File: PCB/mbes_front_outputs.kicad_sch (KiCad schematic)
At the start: 54 parts, among them IC2 BDX34C, IC3 BDX34C, K1 RT42xxxx, Q1 D45VH10, Q10 BC337, Q11 BC337, Q12 BC327, Q13 BC337, Q14 D45VH10, Q15 D45VH10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

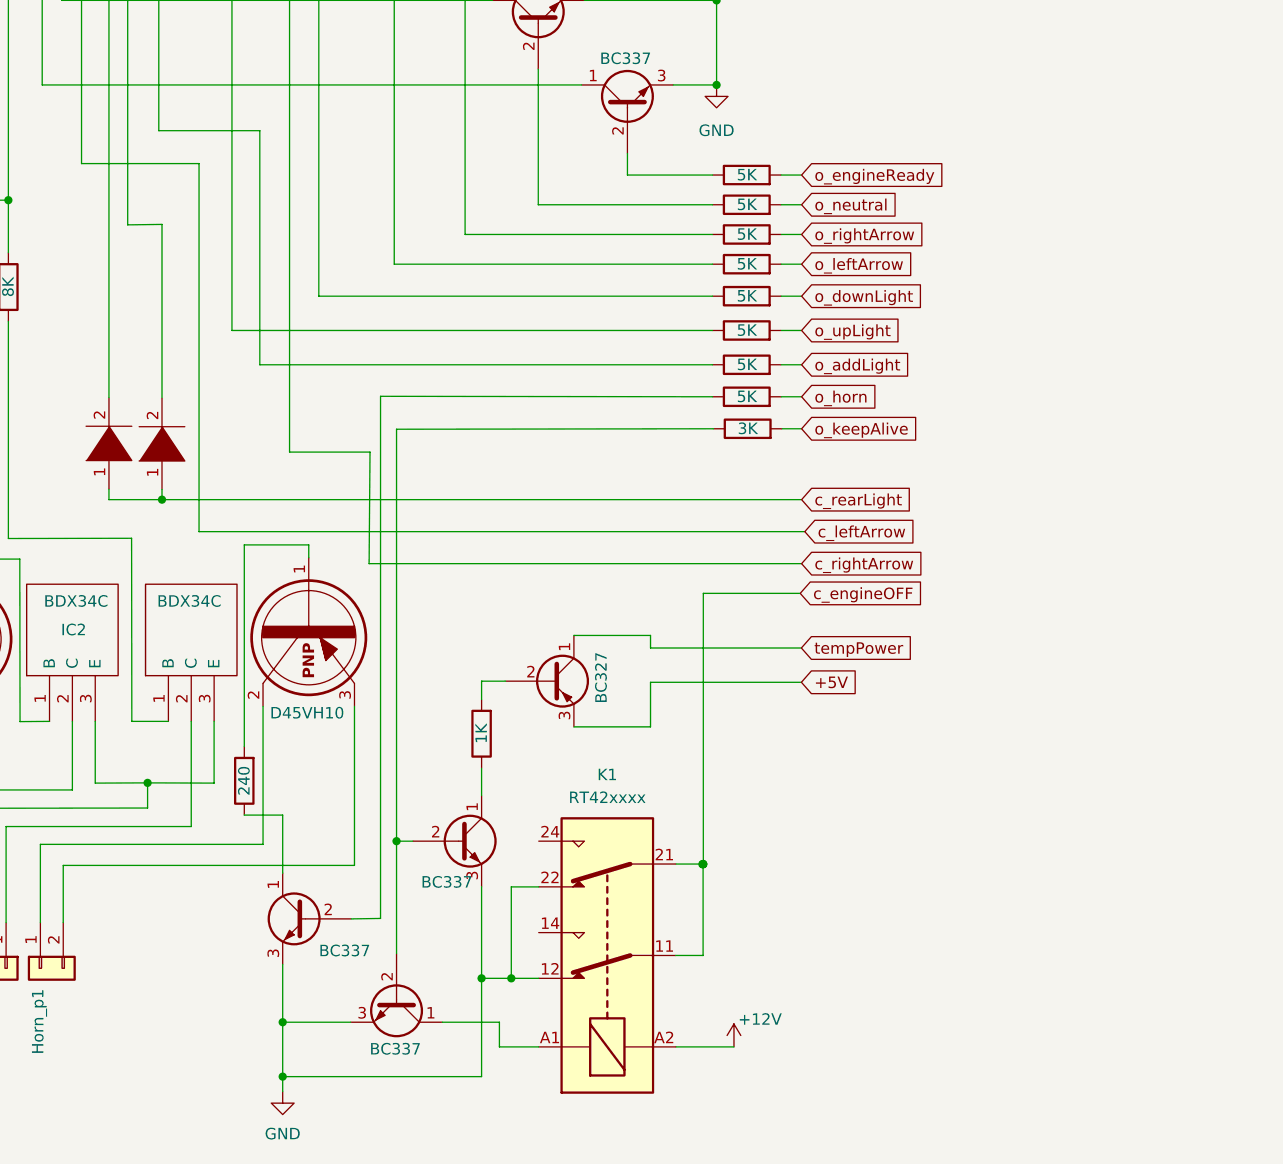
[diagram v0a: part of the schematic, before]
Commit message: feat: power-off button
Because MCU could have a problem for an unpredictable reason, a power-off button has been added to stop the current to the MCU.
But, because I am paranoide and the transistor could have problems, I connected the power-off button yo the MCU too. In this way
it can always shutdown itself
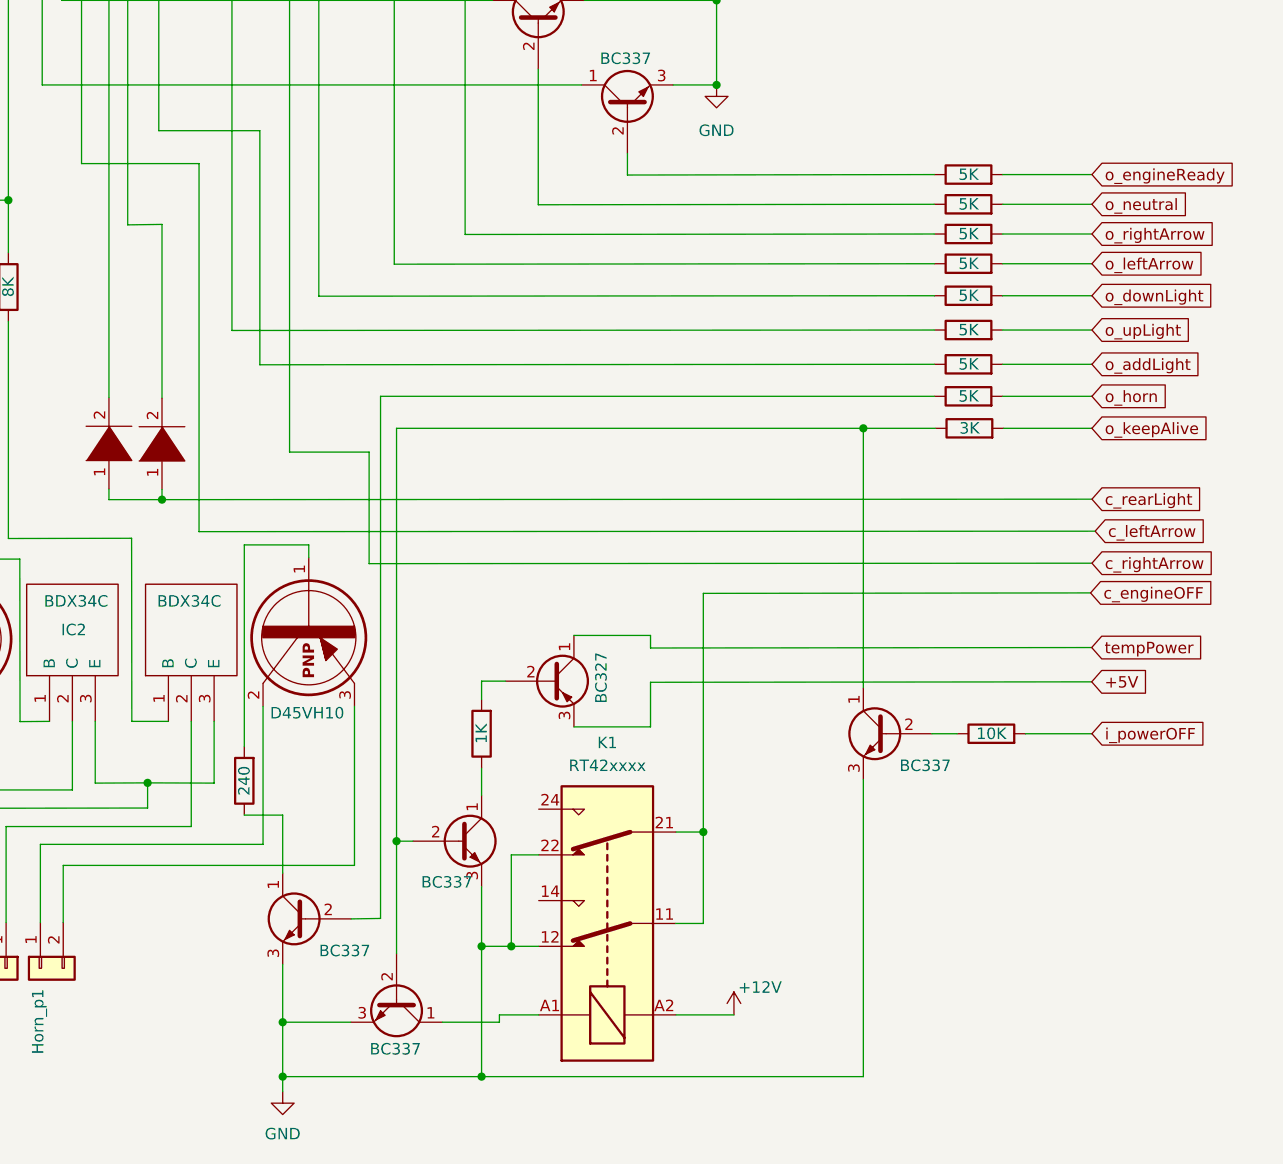
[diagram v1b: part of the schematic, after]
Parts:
- added Q16: BC337, Package_TO_SOT_THT:TO-92L_Inline_Wide, symbol Transistor_BJT:BC337
- added RA29: 10K, Resistor_THT:R_Axial_DIN0207_L6.3mm_D2.5mm_P7.62mm_Horizontal, symbol Device:R
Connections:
- net GND: now also Q16.3 (E)
- net c_rightArrow: now also Q7.1 (C), RA14.1, RA28.2, RA5.1
- net at Q11.2 (B), Q13.2 (B), RA8.1: now also Q16.1 (C)
- new net: Q16.2 (B), RA29.1
- new net i_powerOFF: RA29.2
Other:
- moved on the sheet: K1

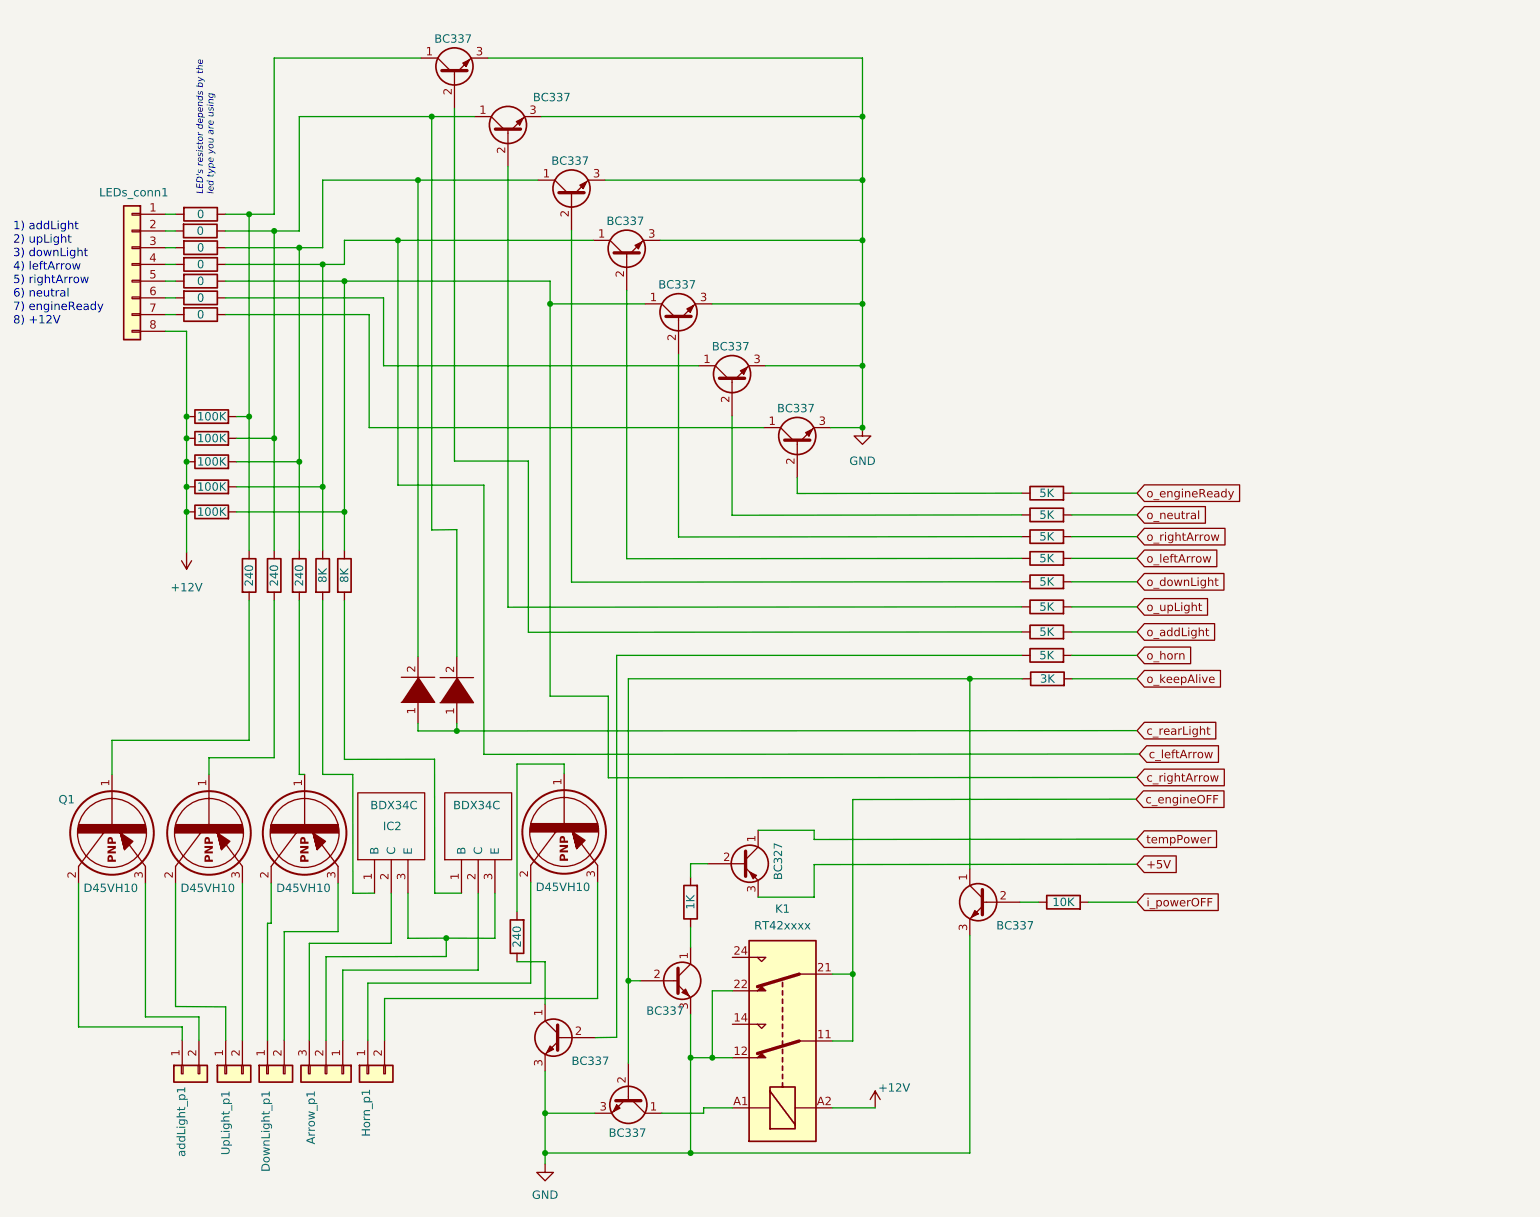
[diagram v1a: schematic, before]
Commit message: Floating BC337 transistors bases fixed, and PowerOFF button management added
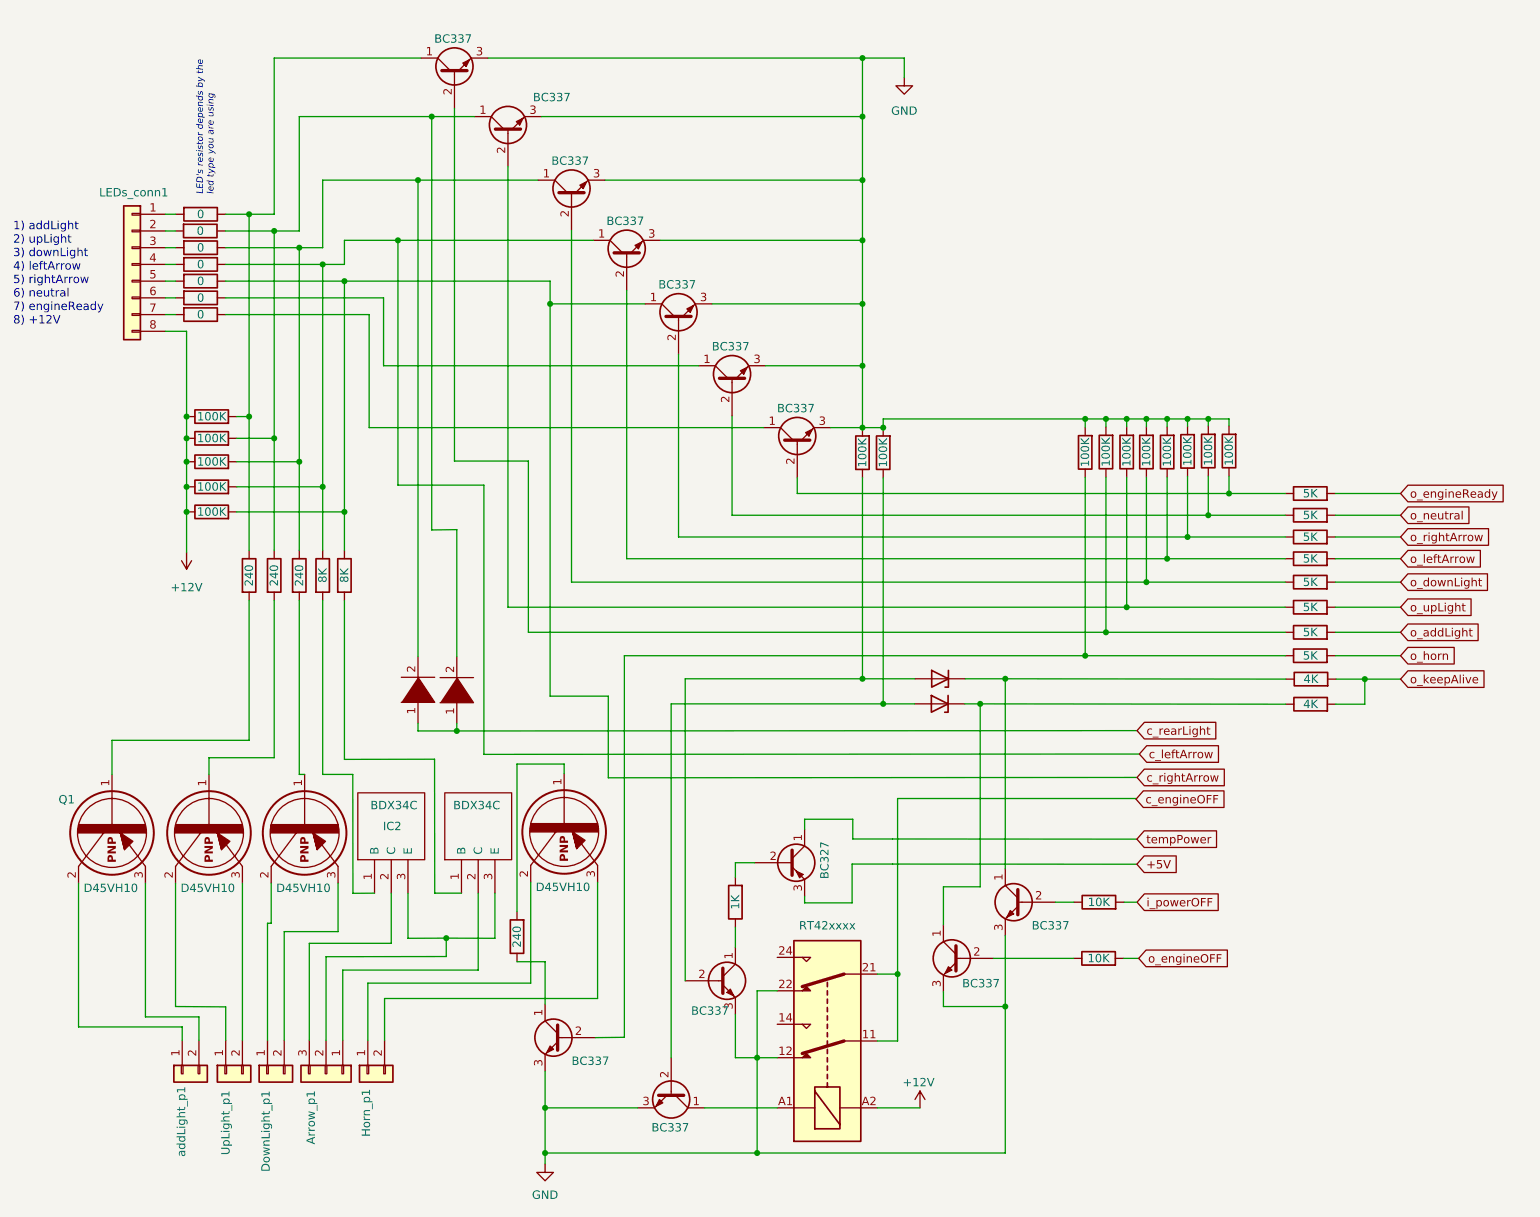
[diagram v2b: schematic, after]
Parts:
- added D3, D4: 2V, Diode_THT:D_DO-35_SOD27_P7.62mm_Horizontal, symbol Diode:BZD27Cxx
- added Q17: BC337, Package_TO_SOT_THT:TO-92L_Inline_Wide, symbol Transistor_BJT:BC337
- added RA30, RA31, RA32, RA34, RA35, RA36, RA37, RA38, RA39, RA40: 100K, Resistor_THT:R_Axial_DIN0207_L6.3mm_D2.5mm_P7.62mm_Horizontal, symbol Device:R
- added RA33: 10K, Resistor_THT:R_Axial_DIN0207_L6.3mm_D2.5mm_P7.62mm_Horizontal, symbol Device:R
- added RA41: 4K, Resistor_THT:R_Axial_DIN0207_L6.3mm_D2.5mm_P7.62mm_Horizontal, symbol Device:R
- RA8: value 3K -> 4K
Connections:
- net GND: now also Q17.3 (E), RA30.2, RA31.2, RA32.2, RA34.2, RA35.2, RA36.2, RA37.2, RA38.2, RA39.2, RA40.2
- net o_keepAlive: now also RA41.2
- net at Q16.1 (C), RA8.1: now also D4.1 (K); no longer Q11.2 (B), Q13.2 (B)
- net at Q9.2 (B), RA23.1: now also RA32.1
- net at Q8.2 (B), RA17.1: now also RA39.1
- net at Q3.2 (B), RA22.1: now also RA34.1
- net at Q6.2 (B), RA19.1: now also RA37.1
- net at Q4.2 (B), RA21.1: now also RA35.1
- net at Q10.2 (B), RA16.1: now also RA40.1
- net at Q5.2 (B), RA20.1: now also RA36.1
- net at Q7.2 (B), RA18.1: now also RA38.1
- new net: D3.1 (K), Q17.1 (C), RA41.1
- new net: Q17.2 (B), RA33.1
- new net: D4.2 (A), Q11.2 (B), RA30.1
- new net: D3.2 (A), Q13.2 (B), RA31.1
- new net o_engineOFF: RA33.2

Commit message: - Other floating BC337 transistors bases fixed - USB port missing fixed - Small enhancements
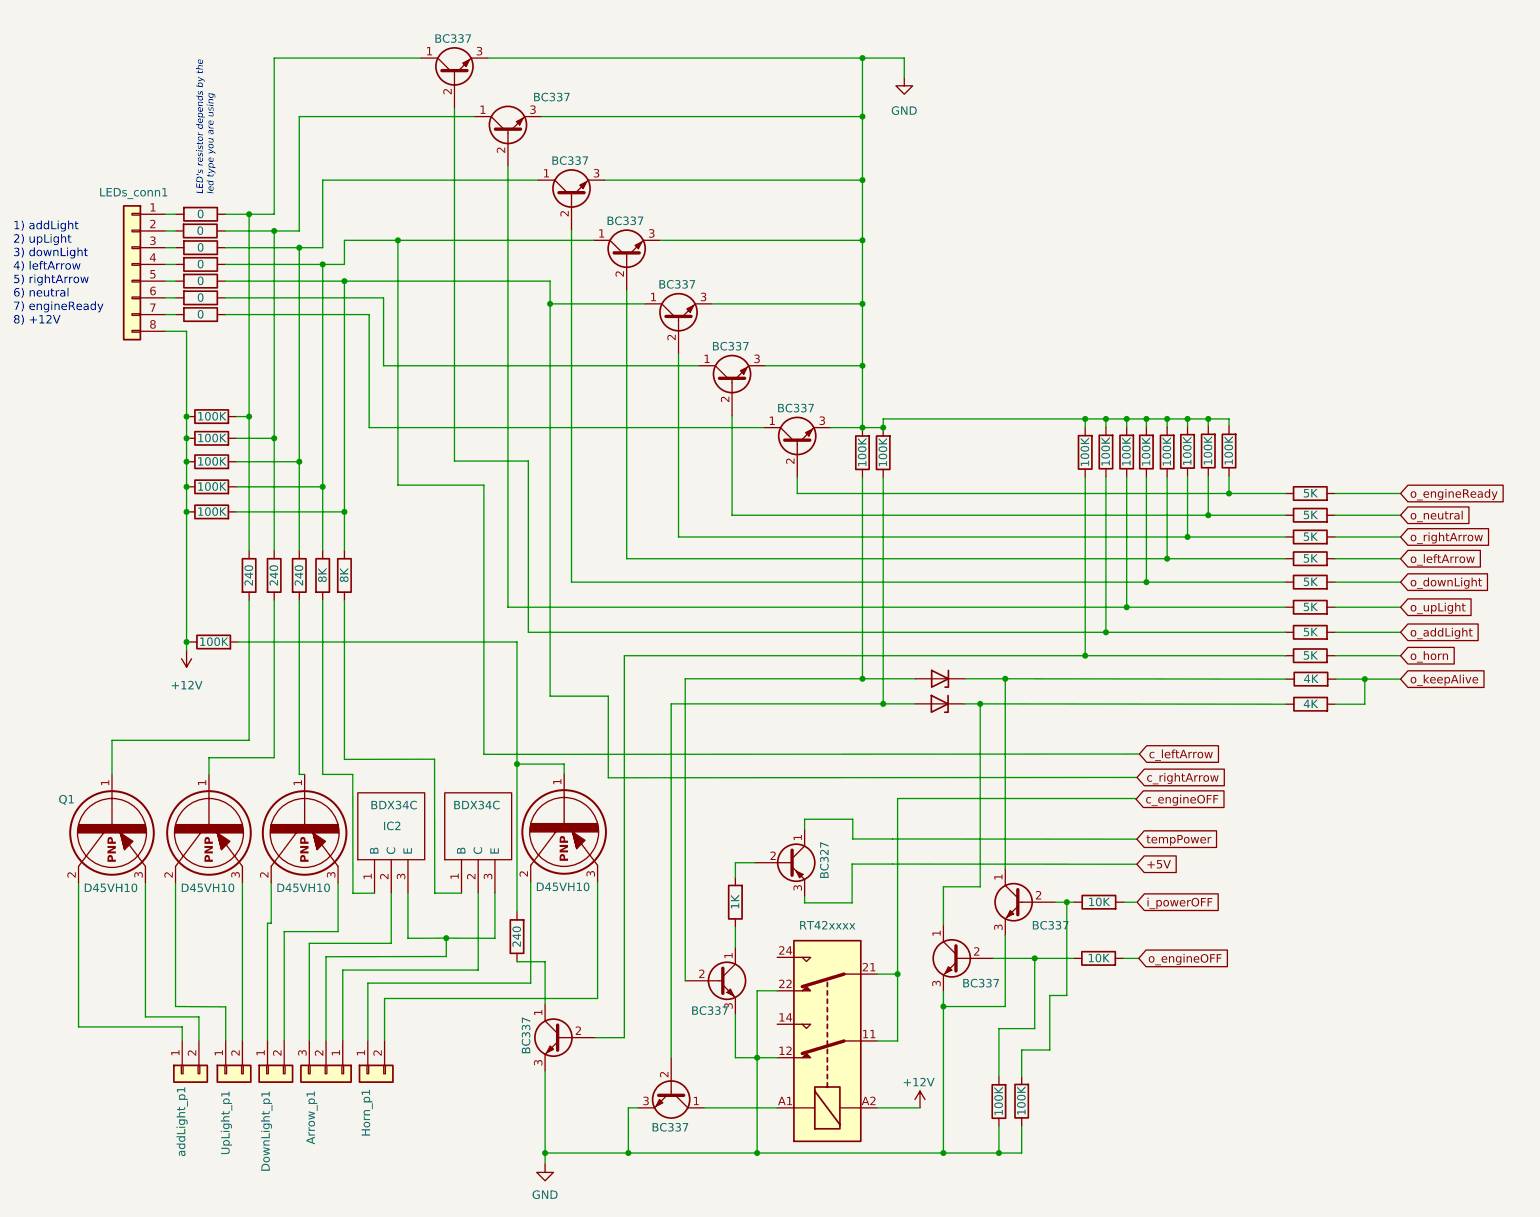
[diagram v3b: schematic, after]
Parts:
- removed D1, D2: DIODE, Diode_THT:D_DO-34_SOD68_P7.62mm_Horizontal, symbol pspice:DIODE
- added RA42, RA43, RA44: 100K, Resistor_THT:R_Axial_DIN0207_L6.3mm_D2.5mm_P7.62mm_Horizontal, symbol Device:R
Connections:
- net +12V: now also RA42.1
- net GND: now also RA43.1, RA44.1
- net at Q15.1, RA15.2: now also RA42.2
- net at Q16.2 (B), RA29.1: now also RA44.2
- net at Q17.2 (B), RA33.1: now also RA43.2
